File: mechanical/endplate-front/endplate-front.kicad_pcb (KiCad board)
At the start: 2 copper layers, 88 x 38 mm, 0 parts

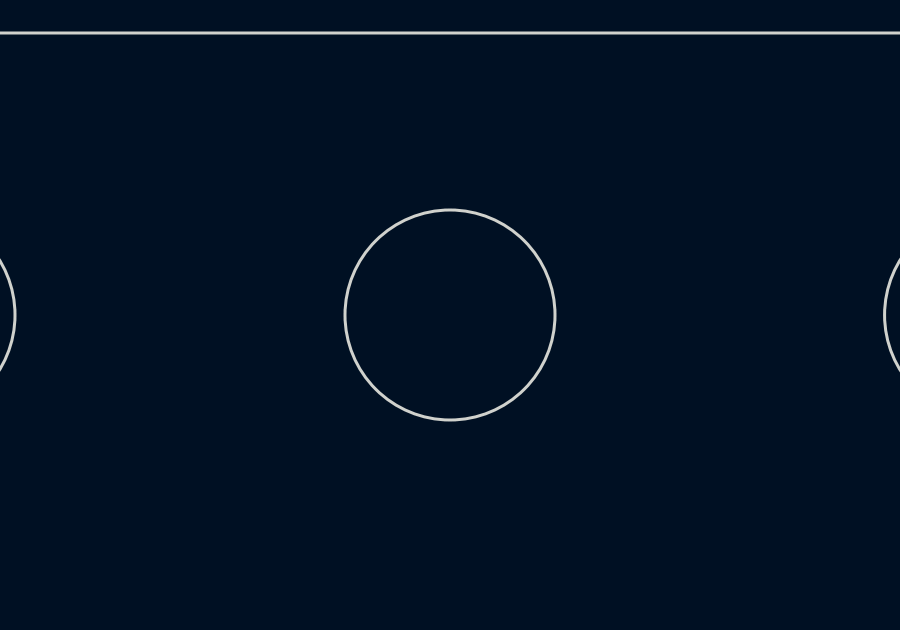
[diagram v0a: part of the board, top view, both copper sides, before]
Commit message: mechanical(endplates): remove the SPARE hole + label (front)
Drop the unused J3/SPARE Ø7.0 panel hole and its silk label from the
front plate; the three active SMA cutouts (RF IN, TIMESYNC IN, EXT REF)
remain. (J3 stays on the board as a spare, just no panel access now.)

Co-Authored-By: Claude Opus 4.8 <noreply@anthropic.com>
Claude-Session: https://claude.ai/code/session_01A68dcoDnizcNYhKvjGet5a
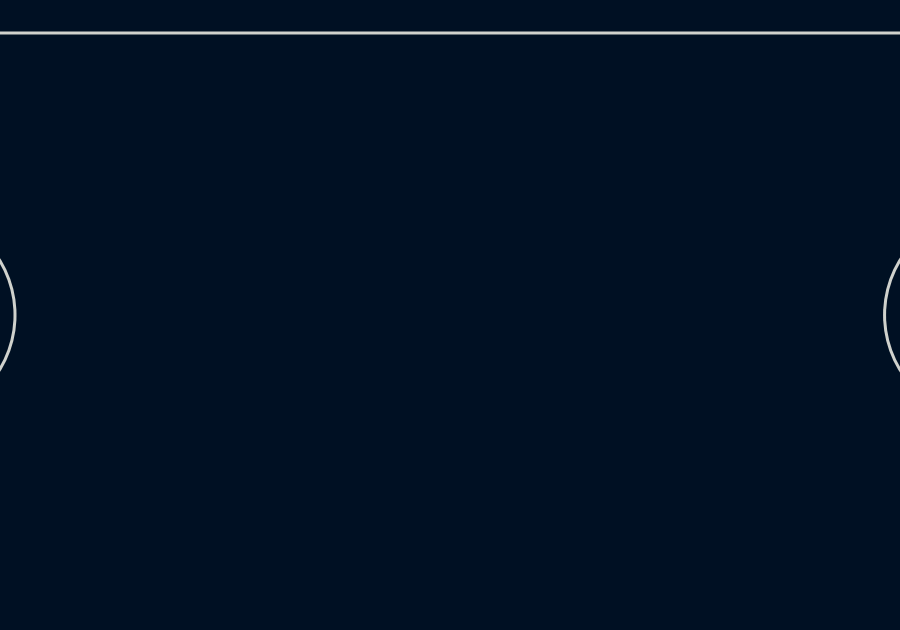
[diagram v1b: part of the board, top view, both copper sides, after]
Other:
- outline, holes or cut-outs redrawn
- board text removed: "SPARE"
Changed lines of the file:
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@@
-	)
-	(gr_circle
-		(center 139.5 95.39)
-		(end 143 95.39)
-		(stroke
-			(width 0.1)
-			(type default)
-		)
-		(fill no)
-		(layer "Edge.Cuts")
 	)
 	(gr_circle
@@
 		(layer "B.SilkS")
 		(effects
-			(font
-				(size 1.25 1.25)
-				(thickness 0.15)
-			)
-			(justify mirror)
-		)
-	)
-	(gr_text "SPARE"
-		(at 139.5 88.89 0)
-		(layer "B.SilkS")
-		(effects

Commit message: mechanical(endplates): refresh Cmts.User notes to as-built geometry
The documentation notes had drifted from the fit-checked geometry. Rewrite
both to match:
- Front: 3 SMA holes Ø7.0 at plate Y 9.40 (RF IN/TIMESYNC IN/EXT REF);
  J3 spare removed (no panel hole); drop the stale rail-height rationale.
- Rear: USB 3.0 opening 12.5x12.9 at plate (25.04,15.49); STATUS Ø2.0 hole
  at (44.0,9.0) for the D3 LED (D3 model +0.5 Z).
Both note plate Y is measured from the floor edge (Y=0, +Y up) and that the
dimensions were dialed in against the 3D fit-check.

Co-Authored-By: Claude Opus 4.8 <noreply@anthropic.com>
Claude-Session: https://claude.ai/code/session_01A68dcoDnizcNYhKvjGet5a
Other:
- board text added: "FRONT PLATE (SMA). Non-functional enclosure end plate. Outline 88x38 R4.5; M3 corner holes Ø3.4 @ +/-41,+/-14.21 (plate screws on, full face). SMA holes Ø7.0 at plate Y 9.40 (fit-checked vs the assembled STEP; plate Y from floor edge Y=0, +Y = up). SMA by plate X: J1=RF IN (17.0), J2=TIMESYNC IN (52.99), J4=EXT REF (70.8). J3 spare has no panel hole. Dimensions dialed in against the 3D fit-check;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"
- board text removed: "Outline+M3 corner holes from enclosure DXF (88x38 R4.5, holes Ø3.4 @ +/-41,+/-14.21). Connector Y set from measured 7.9mm PCB rail height above enclosure floor (TOP edge, Y=0). SMA holes Ø7.0 at plate Y 7.90 (edge-launch, board plane). USB opening 12.5x12.7 at plate Y 14.79 (bottom flush to board top surface; connector rises 12.2 into box). Floor = connector edge (top, Y=0). SMA: J1=RF IN J3=SPAR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"
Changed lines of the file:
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@@
 		)
 	)
-	(gr_text "Outline+M3 corner holes from enclosure DXF (88x38 R4.5, holes Ø3.4 @ +/-41,+/-14.21).\nConnector Y set from measured 7.9mm PCB rail height above enclosure floor (TOP edge, Y=0).\nSMA holes Ø7.0 at plate Y 7.90 (edge-launch, board plane).\nUSB opening 12.5x12.7 at plate Y 14.79 (bottom flush to board top surface; connector rises 12.2 into box).\nFloor = connector edge (top, Y=0).\nSMA: J1=RF IN J3=SPARE J2=TIMESYNC IN J4=EXT REF.\nOpen in KiCad 10 to confirm parse."
+	(gr_text "FRONT PLATE (SMA). Non-functional enclosure end plate.\nOutline 88x38 R4.5; M3 corner holes Ø3.4 @ +/-41,+/-14.21 (plate screws on, full face).\nSMA holes Ø7.0 at plate Y 9.40 (fit-checked vs the assembled STEP; plate Y from floor edge Y=0, +Y = up).\nSMA by plate X: J1=RF IN (17.0), J2=TIMESYNC IN (52.99), J4=EXT REF (70.8). J3 spare has no panel hole.\nDimensions dialed in against the 3D fit-check; open in KiCad 10 to confirm."
 		(at 148.5 133.35 0)
 		(layer "Cmts.User")
